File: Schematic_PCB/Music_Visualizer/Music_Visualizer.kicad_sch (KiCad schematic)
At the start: 131 parts, among them J1 AudioJack2_Ground, SW1 SW_SPDT, U1 LM324, U2 LM324, U3 LM324, U4 LM324, U5 LM324, U6 LM324

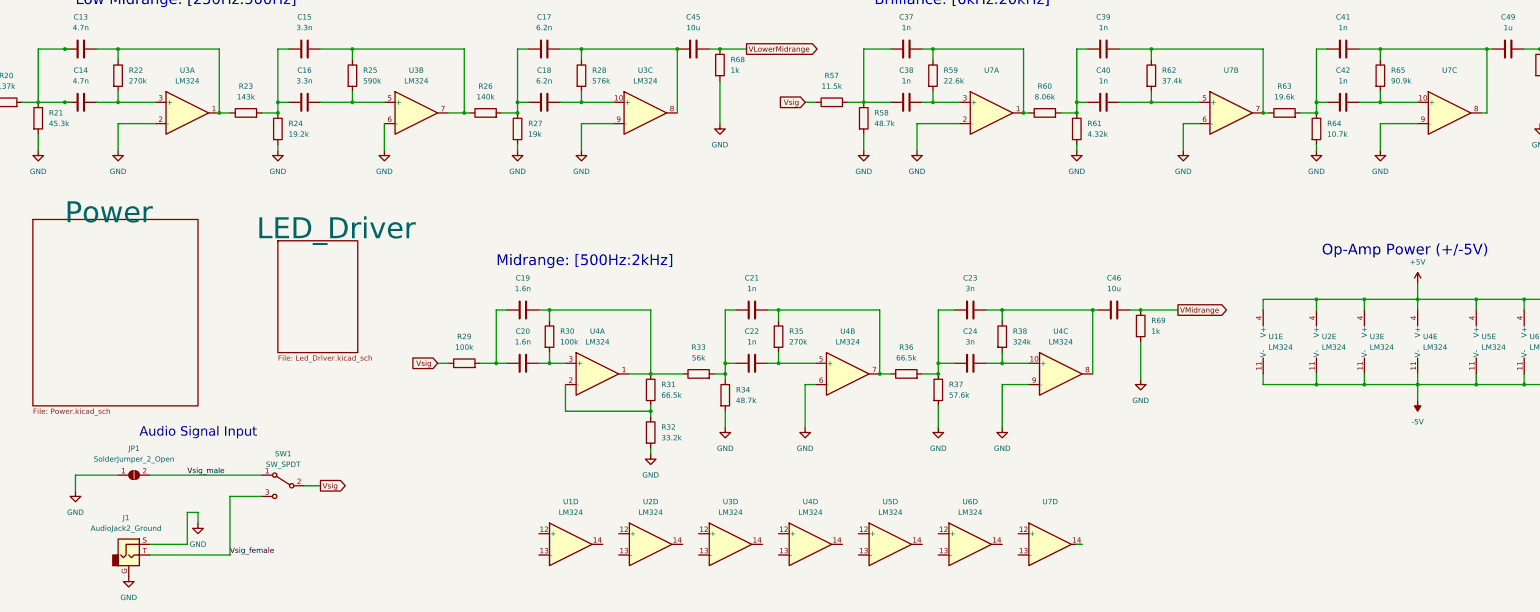
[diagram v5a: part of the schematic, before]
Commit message: Added screw port terminal block to connect male audio jack, traceed audio input and header, all nets have now been traced
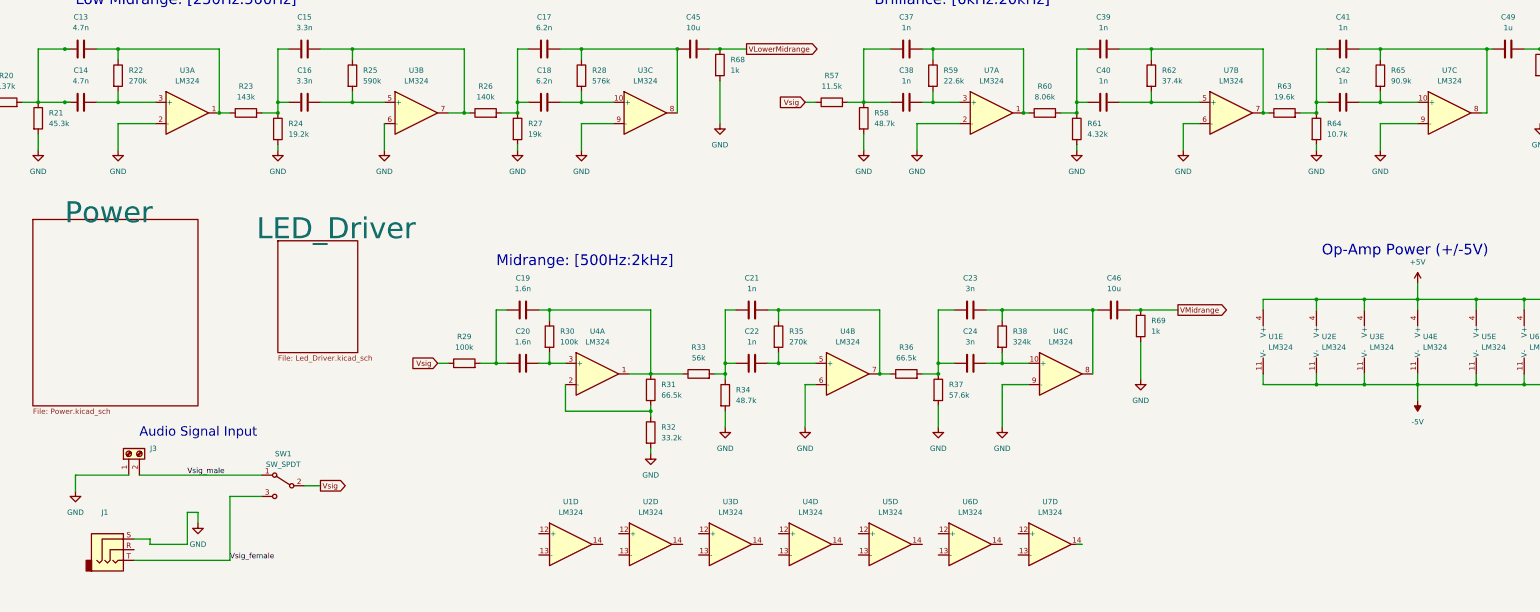
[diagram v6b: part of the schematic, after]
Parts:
- removed J1: AudioJack2_Ground, Connector_Audio:Jack_3.5mm_CUI_SJ-3523-SMT_Horizontal, symbol Connector:AudioJack2_Ground
- removed JP1: SolderJumper_2_Open, Jumper:SolderJumper-2_P1.3mm_Open_Pad1.0x1.5mm, symbol Jumper:SolderJumper_2_Open
- added J1: (no value), symbol Connector:AudioJack3
- added J3: (no value), symbol Connector:Screw_Terminal_01x02
- U7: value (none) -> LM324; footprint (none) -> Package_SO:SOIC-14_3.9x8.7mm_P1.27mm
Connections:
- net GND: now also J1.S, J3.1 (Pin_1)
- net Vsig_female: now also J1.T
- net Vsig_male: now also J3.2 (Pin_2)
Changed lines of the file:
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@@
     (stroke (width 0) (type default) (color 0 0 0 0))
   )
+  (wire (pts (xy 57.15 250.19) (xy 86.36 250.19))
+    (stroke (width 0) (type default) (color 0 0 0 0))
+  )
   (wire (pts (xy 391.16 140.97) (xy 391.16 148.59))
     (stroke (width 0) (type default) (color 0 0 0 0))
@@
     (stroke (width 0) (type default) (color 0 0 0 0))
   )
-  (wire (pts (xy 59.69 269.24) (xy 78.74 269.24))
-    (stroke (width 0) (type default) (color 0 0 0 0))
-  )
   (wire (pts (xy 349.25 208.28) (xy 361.95 208.28))
     (stroke (width 0) (type default) (color 0 0 0 0))
@@
     (stroke (width 0) (type default) (color 0 0 0 0))
   )
-  (wire (pts (xy 78.74 255.27) (xy 78.74 269.24))
+  (wire (pts (xy 78.74 255.27) (xy 78.74 270.51))
     (stroke (width 0) (type default) (color 0 0 0 0))
   )
@@
     (stroke (width 0) (type default) (color 0 0 0 0))
   )
+  (wire (pts (xy 55.88 270.51) (xy 78.74 270.51))
+    (stroke (width 0) (type default) (color 0 0 0 0))
+  )
   (wire (pts (xy 162.56 52.07) (xy 162.56 58.42))
     (stroke (width 0) (type default) (color 0 0 0 0))
@@
     (stroke (width 0) (type default) (color 0 0 0 0))
   )
-  (wire (pts (xy 59.69 250.19) (xy 86.36 250.19))
-    (stroke (width 0) (type default) (color 0 0 0 0))
-  )
   (wire (pts (xy 149.86 161.29) (xy 147.32 161.29))
     (stroke (width 0) (type default) (color 0 0 0 0))
@@
     (stroke (width 0) (type default) (color 0 0 0 0))
   )
+  (wire (pts (xy 59.69 265.43) (xy 59.69 266.7))
+    (stroke (width 0) (type default) (color 0 0 0 0))
+  )
   (wire (pts (xy 267.97 100.33) (xy 269.24 100.33))
     (stroke (width 0) (type default) (color 0 0 0 0))
@@
     (stroke (width 0) (type default) (color 0 0 0 0))
   )
-  (wire (pts (xy 52.07 250.19) (xy 41.91 250.19))
+  (wire (pts (xy 41.91 250.19) (xy 54.61 250.19))
     (stroke (width 0) (type default) (color 0 0 0 0))
   )
@@
     (stroke (width 0) (type default) (color 0 0 0 0))
   )
+  (wire (pts (xy 55.88 265.43) (xy 59.69 265.43))
+    (stroke (width 0) (type default) (color 0 0 0 0))
+  )
   (wire (pts (xy 196.85 223.52) (xy 199.39 223.52))
     (stroke (width 0) (type default) (color 0 0 0 0))
@@
     (effects (font (size 2.54 2.54)) (justify left bottom))
   )
-  (label "Vsig_female" (at 78.74 269.24 0)
+  (label "Vsig_female" (at 78.74 270.51 0)
     (effects (font (size 1.27 1.27)) (justify left bottom))
   )
@@
     (pin "1")
   )
-  (symbol (lib_id "Connector:AudioJack2_Ground") (at 54.61 269.24 0) (unit 1)
-    (in_bom yes) (on_board yes) (fields_autoplaced)
-    (property "Reference" "J1" (id 0) (at 53.975 260.35 0))
-    (property "Value" "AudioJack2_Ground" (id 1) (at 53.975 262.89 0))
-    (property "Footprint" "Connector_Audio:Jack_3.5mm_CUI_SJ-3523-SMT_Horizontal" (id 2) (at 54.61 269.24 0)
-      (effects (font (size 1.27 1.27)) hide)
-    )
-    (property "Datasheet" "~" (id 3) (at 54.61 269.24 0)
-      (effects (font (size 1.27 1.27)) hide)
-    )
-    (pin "G")
-    (pin "S")
-    (pin "T")
-  )
   (symbol (lib_id "Device:R") (at 190.5 226.06 90) (unit 1)
     (in_bom yes) (on_board yes) (fields_autoplaced)
@@
     (in_bom yes) (on_board yes) (fields_autoplaced)
     (property "Reference" "U7" (id 0) (at 369.57 153.67 0))
-    (property "Value" "" (id 1) (at 369.57 156.21 0))
-    (property "Footprint" "" (id 2) (at 368.3 161.29 0)
+    (property "Value" "LM324" (id 1) (at 369.57 156.21 0))
+    (property "Footprint" "Package_SO:SOIC-14_3.9x8.7mm_P1.27mm" (id 2) (at 368.3 161.29 0)
       (effects (font (size 1.27 1.27)) hide)
     )
@@
     (pin "2")
   )
-  (symbol (lib_id "power:GND") (at 54.61 274.32 0) (unit 1)
-    (in_bom yes) (on_board yes) (fields_autoplaced)
-    (property "Reference" "#PWR0102" (id 0) (at 54.61 280.67 0)
-      (effects (font (size 1.27 1.27)) hide)
-    )
-    (property "Value" "GND" (id 1) (at 54.61 279.4 0))
-    (property "Footprint" "" (id 2) (at 54.61 274.32 0)
-      (effects (font (size 1.27 1.27)) hide)
-    )
-    (property "Datasheet" "" (id 3) (at 54.61 274.32 0)
-      (effects (font (size 1.27 1.27)) hide)
-    )
-    (pin "1")
-  )
   (symbol (lib_id "power:GND") (at 229.87 172.72 0) (unit 1)
     (in_bom yes) (on_board yes) (fields_autoplaced)
@@
     (in_bom yes) (on_board yes) (fields_autoplaced)
     (property "Reference" "U7" (id 0) (at 317.5 153.67 0))
-    (property "Value" "" (id 1) (at 317.5 156.21 0))
-    (property "Footprint" "" (id 2) (at 316.23 161.29 0)
+    (property "Value" "LM324" (id 1) (at 317.5 156.21 0))
+    (property "Footprint" "Package_SO:SOIC-14_3.9x8.7mm_P1.27mm" (id 2) (at 316.23 161.29 0)
       (effects (font (size 1.27 1.27)) hide)
     )
@@
     (in_bom yes) (on_board yes) (fields_autoplaced)
     (property "Reference" "U7" (id 0) (at 274.32 256.54 0))
-    (property "Value" "" (id 1) (at 274.32 259.08 0))
-    (property "Footprint" "" (id 2) (at 273.05 264.16 0)
+    (property "Value" "LM324" (id 1) (at 274.32 259.08 0))
+    (property "Footprint" "Package_SO:SOIC-14_3.9x8.7mm_P1.27mm" (id 2) (at 273.05 264.16 0)
       (effects (font (size 1.27 1.27)) hide)
     )
@@
     (pin "2")
   )
+  (symbol (lib_id "Connector:AudioJack3") (at 50.8 267.97 0) (unit 1)
+    (in_bom yes) (on_board yes) (fields_autoplaced)
+    (property "Reference" "J1" (id 0) (at 48.895 259.08 0))
+    (property "Value" "" (id 1) (at 48.895 261.62 0))
+    (property "Footprint" "" (id 2) (at 50.8 267.97 0)
+      (effects (font (size 1.27 1.27)) hide)
+    )
+    (property "Datasheet" "~" (id 3) (at 50.8 267.97 0)
+      (effects (font (size 1.27 1.27)) hide)
+    )
+    (pin "R")
+    (pin "S")
+    (pin "T")
+  )
   (symbol (lib_id "Device:R") (at 337.82 104.14 0) (unit 1)
     (in_bom yes) (on_board yes) (fields_autoplaced)
@@
     (pin "2")
   )
+  (symbol (lib_id "Connector:Screw_Terminal_01x02") (at 54.61 245.11 90) (unit 1)
+    (in_bom yes) (on_board yes) (fields_autoplaced)
+    (property "Reference" "J3" (id 0) (at 59.69 243.8399 90)
+      (effects (font (size 1.27 1.27)) (justify right))
+    )
+    (property "Value" "" (id 1) (at 59.69 246.3799 90)
+      (effects (font (size 1.27 1.27)) (justify right))
+    )
+    (property "Footprint" "" (id 2) (at 54.61 245.11 0)
+      (effects (font (size 1.27 1.27)) hide)
+    )
+    (property "Datasheet" "~" (id 3) (at 54.61 245.11 0)
+      (effects (font (size 1.27 1.27)) hide)
+    )
+    (pin "1")
+    (pin "2")
+  )
   (symbol (lib_id "Amplifier_Operational:LM324") (at 389.89 218.44 0) (unit 5)
     (in_bom yes) (on_board yes) (fields_autoplaced)
@@
     (in_bom yes) (on_board yes) (fields_autoplaced)
     (property "Reference" "U7" (id 0) (at 260.35 153.67 0))
-    (property "Value" "" (id 1) (at 260.35 156.21 0))
-    (property "Footprint" "" (id 2) (at 259.08 161.29 0)
+    (property "Value" "LM324" (id 1) (at 260.35 156.21 0))
+    (property "Footprint" "Package_SO:SOIC-14_3.9x8.7mm_P1.27mm" (id 2) (at 259.08 161.29 0)
       (effects (font (size 1.27 1.27)) hide)
     )
@@
     (pin "4")
   )
-  (symbol (lib_id "Jumper:SolderJumper_2_Open") (at 55.88 250.19 0) (unit 1)
-    (in_bom yes) (on_board yes) (fields_autoplaced)
-    (property "Reference" "JP1" (id 0) (at 55.88 243.84 0))
-    (property "Value" "SolderJumper_2_Open" (id 1) (at 55.88 246.38 0))
-    (property "Footprint" "Jumper:SolderJumper-2_P1.3mm_Open_Pad1.0x1.5mm" (id 2) (at 55.88 250.19 0)
-      (effects (font (size 1.27 1.27)) hide)
-    )
-    (property "Datasheet" "~" (id 3) (at 55.88 250.19 0)
-      (effects (font (size 1.27 1.27)) hide)
-    )
-    (pin "1")
-    (pin "2")
-  )
   (symbol (lib_id "Device:R") (at 179.07 229.87 0) (unit 1)
     (in_bom yes) (on_board yes) (fields_autoplaced)
@@
       (reference "#PWR0101") (unit 1) (value "GND") (footprint "")
     )
-    (path "/bd78d920-ce8f-46c0-be64-717c08a69612"
-      (reference "#PWR0102") (unit 1) (value "GND") (footprint "")
-    )
     (path "/56ed3a67-eed8-4688-8767-d6bf63bd87ca/f1e7842c-38bd-4f26-8b9c-e130e7c2a1e9"
       (reference "#PWR0103") (unit 1) (value "GND") (footprint "")
@@
       (reference "D71") (unit 1) (value "LED") (footprint "LED_THT:LED_D5.0mm")
     )
-    (path "/5fded386-4830-4c6d-a6ca-3b530b67ab9c"
-      (reference "J1") (unit 1) (value "AudioJack2_Ground") (footprint "Connector_Audio:Jack_3.5mm_CUI_SJ-3523-SMT_Horizontal")
+    (path "/def582bd-912f-4d18-9891-685b277a4c3f"
+      (reference "J1") (unit 1) (value "AudioJack3") (footprint "Connector_Audio:Jack_3.5mm_CUI_SJ-3523-SMT_Horizontal")
     )
     (path "/d77592bc-5812-4255-9ac4-28fcc93efec5/e49cfd4a-442e-4c4e-a4e7-e091c087c649"
       (reference "J2") (unit 1) (value "PJ-079BH") (footprint "CUI_PJ-079BH")
     )
-    (path "/ed6fe133-376d-4373-a2a8-b598ebc0c295"
-      (reference "JP1") (unit 1) (value "SolderJumper_2_Open") (footprint "Jumper:SolderJumper-2_P1.3mm_Open_Pad1.0x1.5mm")
+    (path "/e129812e-54c7-4cd3-b0df-4b1235210535"
+      (reference "J3") (unit 1) (value "Screw_Terminal_01x02") (footprint "TerminalBlock_Phoenix:TerminalBlock_Phoenix_MPT-0,5-2-2.54_1x02_P2.54mm_Horizontal")
     )
     (path "/56ed3a67-eed8-4688-8767-d6bf63bd87ca/d196db43-8ddb-414f-b9f6-73c647803a2e"

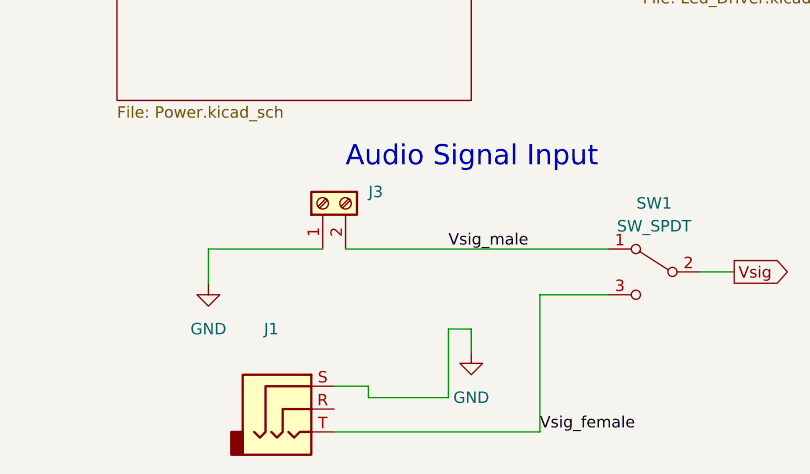
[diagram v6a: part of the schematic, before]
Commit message: Re-oriented Power Indicator circuit
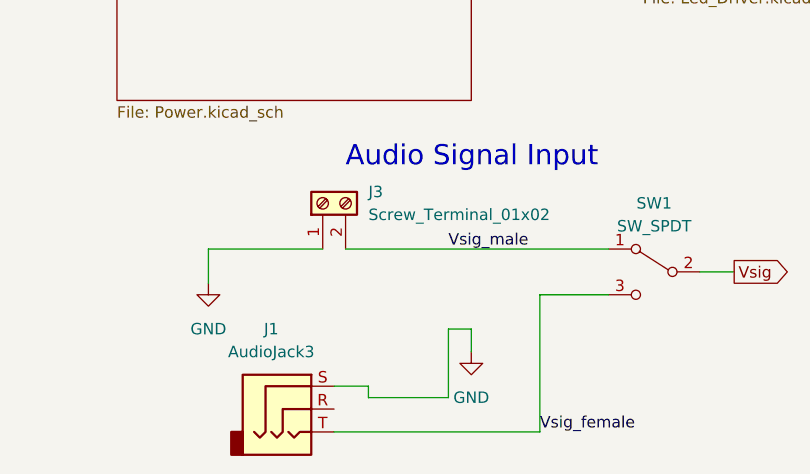
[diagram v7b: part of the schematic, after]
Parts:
- J1: value (none) -> AudioJack3; footprint (none) -> Connector_Audio:Jack_3.5mm_CUI_SJ-3523-SMT_Horizontal
- J3: value (none) -> Screw_Terminal_01x02; footprint (none) -> TerminalBlock_Phoenix:TerminalBlock_Phoenix_MPT-0,5-2-2.54_1x02_P2.54mm_Horizontal
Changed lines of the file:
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@@
     (in_bom yes) (on_board yes) (fields_autoplaced)
     (property "Reference" "J1" (id 0) (at 48.895 259.08 0))
-    (property "Value" "" (id 1) (at 48.895 261.62 0))
-    (property "Footprint" "" (id 2) (at 50.8 267.97 0)
+    (property "Value" "AudioJack3" (id 1) (at 48.895 261.62 0))
+    (property "Footprint" "Connector_Audio:Jack_3.5mm_CUI_SJ-3523-SMT_Horizontal" (id 2) (at 50.8 267.97 0)
       (effects (font (size 1.27 1.27)) hide)
     )
@@
       (effects (font (size 1.27 1.27)) (justify right))
     )
-    (property "Value" "" (id 1) (at 59.69 246.3799 90)
+    (property "Value" "Screw_Terminal_01x02" (id 1) (at 59.69 246.3799 90)
       (effects (font (size 1.27 1.27)) (justify right))
     )
-    (property "Footprint" "" (id 2) (at 54.61 245.11 0)
+    (property "Footprint" "TerminalBlock_Phoenix:TerminalBlock_Phoenix_MPT-0,5-2-2.54_1x02_P2.54mm_Horizontal" (id 2) (at 54.61 245.11 0)
       (effects (font (size 1.27 1.27)) hide)
     )

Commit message: Added 0.1uF decoupling capacitors to the op-amps on the schematic and placed and traced on the PCB
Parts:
- added C60, C61, C62, C63, C64, C65, C66, C67, C68, C69, C70, C71, C72, C73: 0.1uF, Capacitor_SMD:C_0805_2012Metric, symbol Device:C
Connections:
- net +5V: now also C60.2, C62.2, C64.2, C66.2, C68.2, C70.2, C72.2
- net -5V: now also C61.1, C63.1, C65.1, C67.1, C69.1, C71.1, C73.1
- net GND: now also C60.1, C61.2, C62.1, C63.2, C64.1, C65.2, C66.1, C67.2, C68.1, C69.2, C70.1, C71.2, C72.1, C73.2
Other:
- moved on the sheet: C1, C10, C11, C12, C13, C14, C15, C16, C17, C18, C19, C2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
